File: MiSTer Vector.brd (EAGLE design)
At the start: 80.4 x 63.9 mm, 49 parts, among them CON2 22-23-2021, IC1 74HC00D, IC2 TL084, IC3 TL084, IC7 MAX6105, U1 MCP4922, U2 MCP4922, U3 MCP4922, U8 VASD1-SIP, X2 ILDA 25 Pin

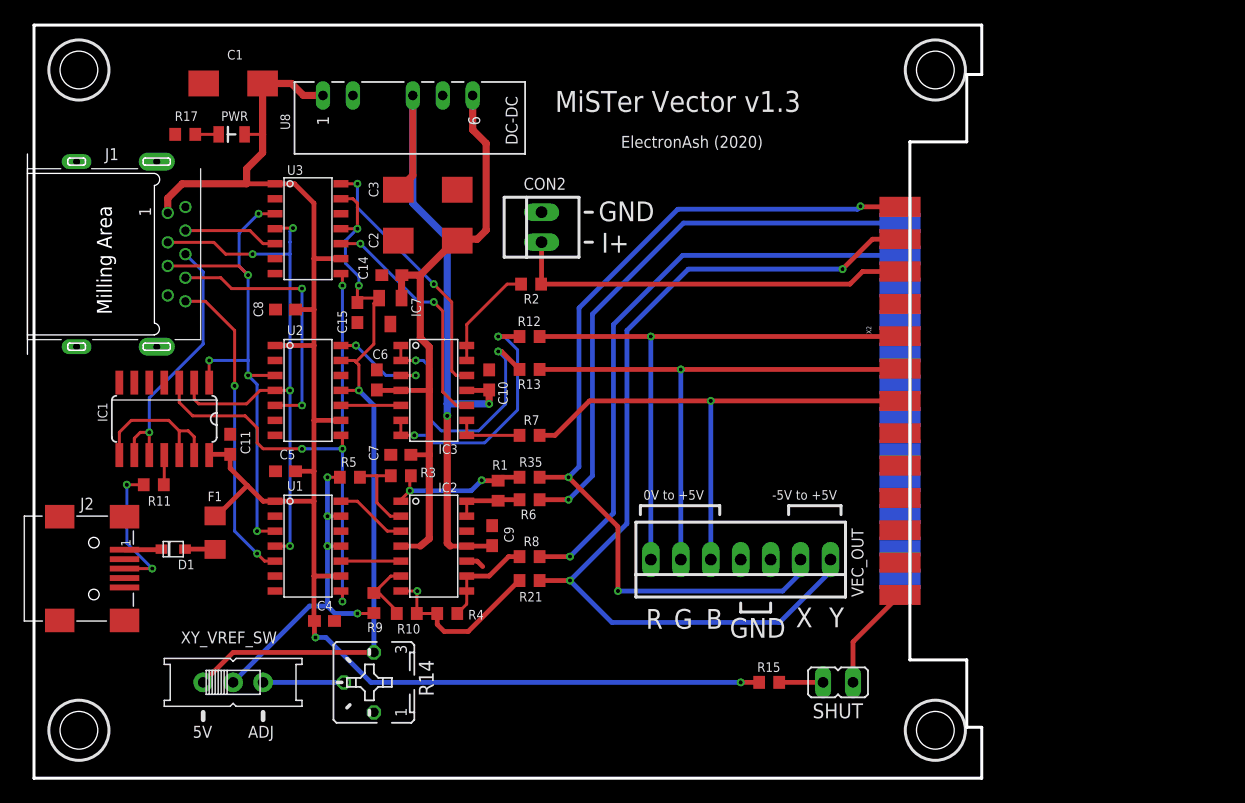
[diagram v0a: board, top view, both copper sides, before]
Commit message: added size adjustment for Molex output. ILDA fixed to 0-5V
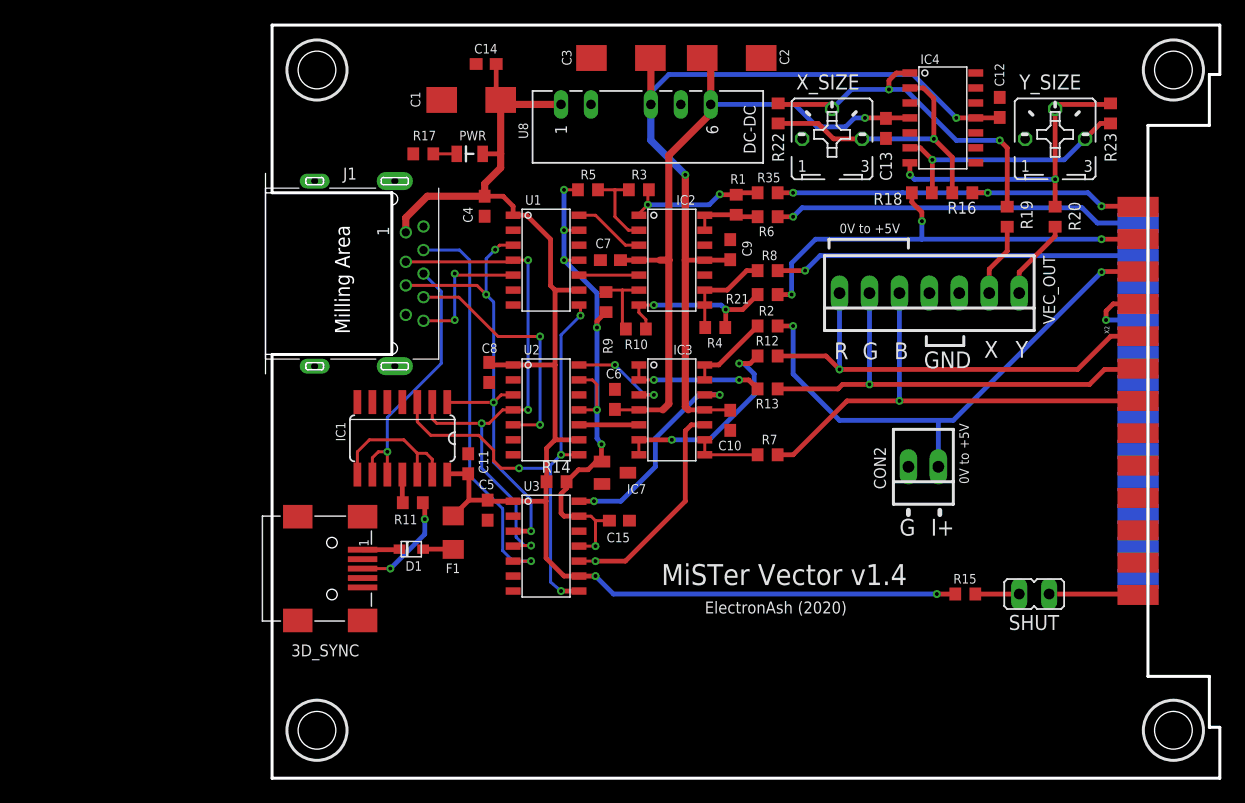
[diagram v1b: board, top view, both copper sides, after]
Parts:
- removed J2: (no value), 632723100011_Eagle_WR-USB_rev19b:65100516121
- removed XY_VREF_SW: (no value), adafruit:EG1218
- added 3D_SYNC: (no value), 632723100011_Eagle_WR-USB_rev19b:65100516121
- added C12, C13: 0.1uF, adafruit:C0603
- added IC4: TL084, favreau:SOIC-14
- added R16, R18, R19, R20: 75R, resistor:R0603
- added R22, R23: 10K, resistor:R0603
- added X_SIZE, Y_SIZE: 20K, pot:B25P
- IC7: value MAX6105 -> LM4040C25FTA
- R14: value (none) -> 100R; device pot:B25P -> rcl:R0603
- moved CON2 38.2 mm to (55.2, 26.4), turned to 180 degrees
- moved C4 37.7 mm to (18.0, 48.5), turned to 270 degrees
- moved U3 33.7 mm to (21.2, 24.0)
- moved R4 33.2 mm to (37.6, 38.2), turned to 180 degrees
- moved R9 32.2 mm to (28.3, 40.4)
- moved R5 31.7 mm to (26.8, 49.9)
- moved C9 31.6 mm to (38.9, 44.8)
- moved IC2 31.6 mm to (31.9, 48.3)
- moved R1 31.6 mm to (39.4, 48.6)
- moved R21 31.6 mm to (42.0, 41.0)
- moved R3 31.6 mm to (31.1, 49.9)
- moved R8 31.6 mm to (42.0, 43.1)
- moved U1 31.6 mm to (21.2, 48.3)
- moved R35 31.5 mm to (42.0, 49.7)
- moved R6 31.4 mm to (42.0, 47.6)
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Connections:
- removed net +VREF_XY: R5.1, R9.1, U1.11, U1.13, XY_VREF_SW.P
- removed net N$13: R14.S, XY_VREF_SW.S
- new net N$14: IC4.2, R16.2, R22.1, X_SIZE.E
- new net N$15: IC4.6, R18.2, R23.1, Y_SIZE.E
- new net N$16: IC4.7, R20.1, R23.2, Y_SIZE.S
- new net N$17: IC4.1, R19.1, R22.2, X_SIZE.S
- new net VEC_X+: R19.2, VEC_OUT.2
- new net VEC_Y+: R20.2, VEC_OUT.1
- net +12V: now also C13.1, IC4.4; no longer C14.1, IC7.1
- net +5V: now also C14.1, R14.1
- net +VREF: now also IC7.1, R14.2, R5.1, R9.1, U1.11, U1.13; no longer IC7.2, R14.E, XY_VREF_SW.O
- net -12V: now also C12.2, IC4.11
- net GND: now also 3D_SYNC.5, 3D_SYNC.SHELL, 3D_SYNC.SHELL1, 3D_SYNC.SHELL2, 3D_SYNC.SHELL3, C12.1, C13.2, IC4.3, IC4.5, IC7.2; no longer J2.5, J2.SHELL, J2.SHELL1, J2.SHELL2, J2.SHELL3, R14.A
- net N$6: now also 3D_SYNC.1; no longer J2.1
- net N$9: now also 3D_SYNC.3; no longer J2.3
- net X+: now also R16.1; no longer VEC_OUT.2
- net Y+: now also R18.1; no longer VEC_OUT.1
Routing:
- net X+: track 76.7 -> 32.7 mm
- net Y+: track 78.5 -> 38.4 mm, vias 2 -> 3
- net N$17: track 0.00 -> 30.2 mm, vias 0 -> 2
- net +VREF_XY: track 29.2 -> 0.00 mm, vias 4 -> 0
- net N$16: track 0.00 -> 26.7 mm, vias 0 -> 2
- net DAC_BI_DAT: track 8.06 -> 34.4 mm, vias 0 -> 1
- net N$14: track 0.00 -> 24.8 mm, vias 0 -> 1
- net N$15: track 0.00 -> 21.5 mm, vias 0 -> 1
- net Y-: track 50.5 -> 31.1 mm
- net X-: track 48.4 -> 31.5 mm
- net DAC_XY_DAT: track 26.7 -> 11.6 mm
- net +VREF: track 64.3 -> 49.6 mm, vias 3 -> 7
- net +5V: track 135.4 -> 121.0 mm
- net -12V: track 58.3 -> 71.3 mm
- net G1+: track 23.3 -> 11.7 mm
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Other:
- outline, holes or cut-outs redrawn
- board text added: "MiSTer Vector v1.4"
- board text removed: "-5V to +5V"
- board text removed: "ADJ"
- board text removed: "MiSTer Vector v1.3"

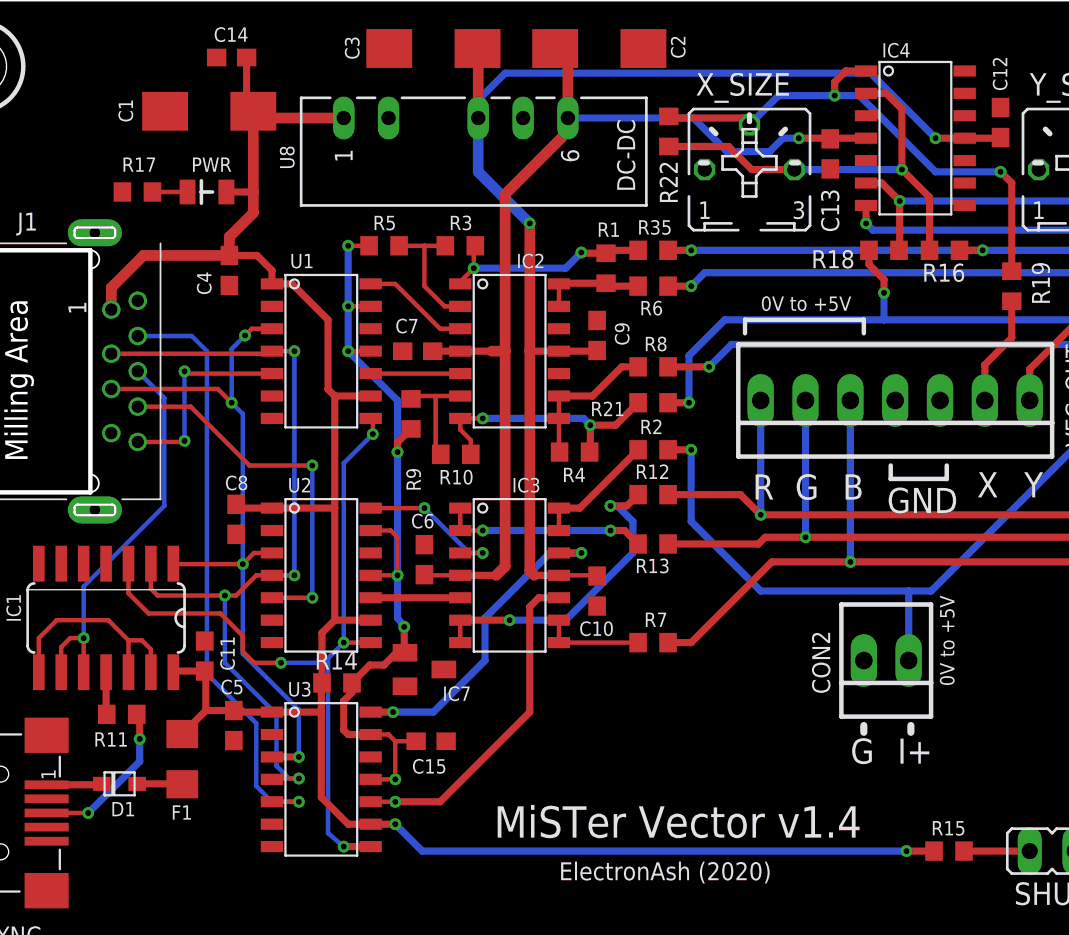
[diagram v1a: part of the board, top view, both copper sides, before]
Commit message: swapped USBIO TX/RX pairs, as done in most USB3 TypeA-TypeA cables
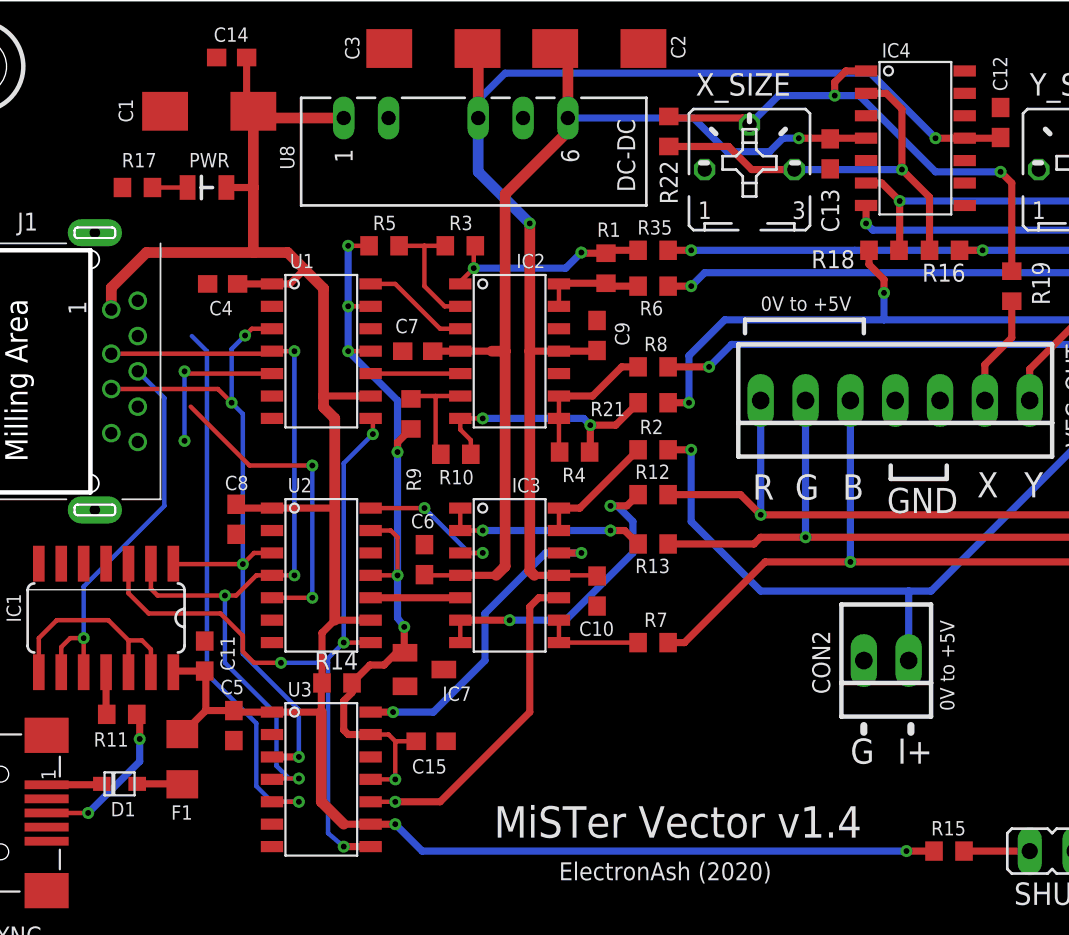
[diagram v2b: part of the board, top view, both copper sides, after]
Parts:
- moved C4 0.85 mm to (17.7, 47.8), turned to 180 degrees
- moved PWR 0.25 mm to (16.8, 53.2)
- moved R17 0.25 mm to (12.8, 53.2)
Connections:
- net +3V3: now also J1.6; no longer J1.9
- net DAC_BI_DAT: now also J1.5; no longer J1.8
- net DAC_RG_DAT: now also J1.9; no longer J1.6
- net DAC_XY_DAT: now also J1.8; no longer J1.5
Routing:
- net +5V: track 121.0 -> 125.6 mm
- net DAC_BI_DAT: track 34.4 -> 31.3 mm
- net DAC_RG_DAT: track 21.0 -> 18.0 mm
- net DAC_XY_DAT: track 11.6 -> 9.03 mm

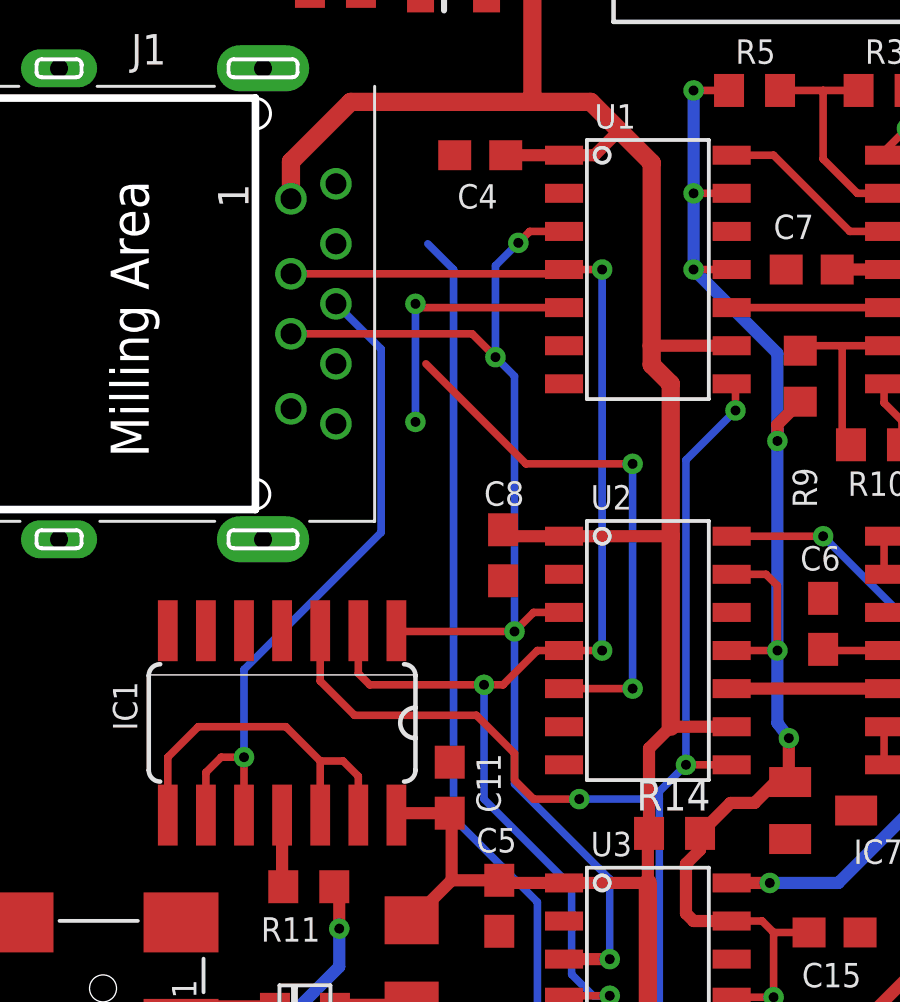
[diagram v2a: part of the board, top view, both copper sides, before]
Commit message: routed the swapped TX/RX pairs on USBIO
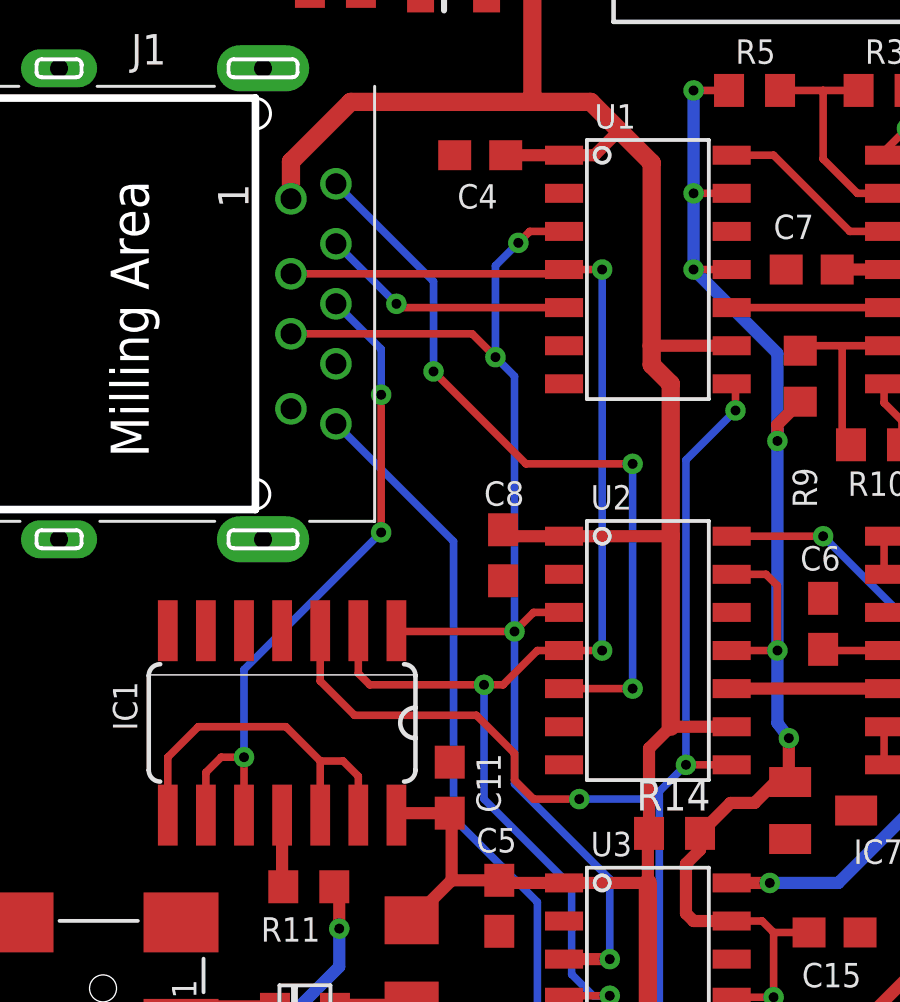
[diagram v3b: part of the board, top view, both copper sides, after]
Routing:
- net DAC_RG_DAT: track 18.0 -> 25.3 mm, vias 2 -> 3
- net DAC_BI_DAT: track 31.3 -> 26.6 mm
- net DAC_XY_DAT: track 9.03 -> 8.48 mm, vias 2 -> 1
- net 3D_SYNC_USBIO: vias 1 -> 3
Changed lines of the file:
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@@
 <wire x1="22.733" y1="37.465" x2="22.733" y2="29.972" width="0.254" layer="16"/>
 <wire x1="19.177" y1="37.465" x2="22.733" y2="37.465" width="0.254" layer="1"/>
-<wire x1="15.843" y1="40.799" x2="19.177" y2="37.465" width="0.254" layer="1"/>
+<wire x1="16.097" y1="40.545" x2="19.177" y2="37.465" width="0.254" layer="1"/>
 <contactref element="J1" pad="9"/>
-<wire x1="15.843" y1="40.799" x2="12.844" y2="46.799" width="0" layer="19" extent="1-1"/>
+<via x="16.097" y="40.545" extent="1-16" drill="0.3302"/>
+<wire x1="16.097" y1="40.545" x2="16.097" y2="43.546" width="0.254" layer="16"/>
+<wire x1="16.097" y1="43.546" x2="12.844" y2="46.799" width="0.254" layer="16"/>
 </signal>
 <signal name="SPI_CLK">
@@
 <signal name="DAC_BI_DAT">
 <contactref element="U3" pad="5"/>
-<wire x1="15.907" y1="44.799" x2="16.764" y2="43.942" width="0.254" layer="16"/>
-<wire x1="16.764" y1="43.942" x2="16.764" y2="25.654" width="0.254" layer="16"/>
 <wire x1="16.764" y1="25.654" x2="19.558" y2="22.86" width="0.254" layer="16"/>
 <wire x1="19.558" y1="22.86" x2="19.558" y2="19.304" width="0.254" layer="16"/>
@@
 <wire x1="21.971" y1="18.415" x2="20.447" y2="18.415" width="0.254" layer="1"/>
 <contactref element="J1" pad="5"/>
-<wire x1="16.764" y1="43.942" x2="12.844" y2="38.799" width="0" layer="19" extent="16-16"/>
+<wire x1="16.764" y1="25.654" x2="16.764" y2="34.879" width="0.254" layer="16"/>
+<wire x1="16.764" y1="34.879" x2="12.844" y2="38.799" width="0.254" layer="16"/>
 </signal>
 <signal name="DAC_XY_DAT">
 <contactref element="U1" pad="5"/>
-<wire x1="20.447" y1="42.672" x2="15.621" y2="42.672" width="0.254" layer="1"/>
-<wire x1="15.621" y1="42.672" x2="15.494" y2="42.799" width="0.254" layer="1"/>
-<via x="15.494" y="42.799" extent="1-16" drill="0.3302"/>
-<wire x1="15.494" y1="42.799" x2="15.494" y2="38.862" width="0.254" layer="16"/>
-<via x="15.494" y="38.862" extent="1-16" drill="0.3302"/>
-<wire x1="15.494" y1="38.862" x2="15.431" y2="38.799" width="0.254" layer="1"/>
+<wire x1="20.447" y1="42.672" x2="14.986" y2="42.672" width="0.254" layer="1"/>
+<wire x1="14.986" y1="42.672" x2="14.859" y2="42.799" width="0.254" layer="1"/>
+<via x="14.859" y="42.799" extent="1-16" drill="0.3302"/>
 <contactref element="J1" pad="8"/>
-<wire x1="15.494" y1="42.799" x2="12.844" y2="44.799" width="0" layer="19" extent="1-1"/>
+<wire x1="14.859" y1="42.799" x2="12.859" y2="44.799" width="0.254" layer="16"/>
+<wire x1="12.859" y1="44.799" x2="12.844" y2="44.799" width="0.254" layer="16"/>
 </signal>
 <signal name="3D_SYNC_USBIO">
@@
 <via x="9.779" y="27.686" extent="1-16" drill="0.3302"/>
 <contactref element="J1" pad="7"/>
-<wire x1="12.844" y1="42.799" x2="14.351" y2="41.292" width="0.254" layer="16"/>
-<wire x1="14.351" y1="41.292" x2="14.351" y2="35.179" width="0.254" layer="16"/>
 <wire x1="14.351" y1="35.179" x2="9.779" y2="30.607" width="0.254" layer="16"/>
 <wire x1="9.779" y1="25.7556" x2="9.779" y2="27.686" width="0.254" layer="1"/>
@@
 <wire x1="8.509" y1="27.178" x2="9.017" y2="27.686" width="0.254" layer="1"/>
 <wire x1="9.017" y1="27.686" x2="9.779" y2="27.686" width="0.254" layer="1"/>
+<via x="14.351" y="35.179" extent="1-16" drill="0.3302"/>
+<wire x1="14.351" y1="35.179" x2="14.351" y2="39.768" width="0.254" layer="1"/>
+<via x="14.351" y="39.768" extent="1-16" drill="0.3302"/>
+<wire x1="12.844" y1="42.799" x2="14.351" y2="41.292" width="0.254" layer="16"/>
+<wire x1="14.351" y1="41.292" x2="14.351" y2="39.768" width="0.254" layer="16"/>
 </signal>
 <signal name="N$8">
